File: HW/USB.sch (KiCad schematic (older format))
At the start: 6 parts

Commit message: remove pin from USB
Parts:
- removed D?: D_Schottky, symbol Device:D_Schottky
- removed J?: +5V_USB, symbol Connector:Conn_01x01_Male
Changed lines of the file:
@@
 $Descr A4 11693 8268
 encoding utf-8
-Sheet 17 42
+Sheet 15 42
 Title ""
 Date ""
@@
 	4300 3250 4350 3250
 Wire Wire Line
-	4300 2950 4400 2950
+	4300 2950 4650 2950
 $Comp
 L Diode:SD05_SOD323 D?
@@
 	4500 3150 4300 3150
 $Comp
-L Device:D_Schottky D?
-U 1 1 5F7931B4
-P 4650 2650
-AR Path="/5FBB3550/5F7931B4" Ref="D?"  Part="1"
-AR Path="/5F7931B4" Ref="D?"  Part="1"
-AR Path="/5F78DB3E/5F7931B4" Ref="D?"  Part="1"
-F 0 "D?" V 4604 2730 50  0000 L CNN
-F 1 "D_Schottky" V 4695 2730 50  0000 L CNN
-F 2 "" H 4650 2650 50  0001 C CNN
-F 3 "~" H 4650 2650 50  0001 C CNN
-	1    4650 2650
-	0    1    1    0
-$EndComp
-Wire Wire Line
-	4650 2800 4650 2950
-$Comp
-L Connector:Conn_01x01_Male J?
-U 1 1 5F7931BB
-P 4650 2150
-AR Path="/5FBB3550/5F7931BB" Ref="J?"  Part="1"
-AR Path="/5F7931BB" Ref="J?"  Part="1"
-AR Path="/5F78DB3E/5F7931BB" Ref="J?"  Part="1"
-F 0 "J?" V 4712 2194 50  0000 L CNN
-F 1 "+5V_USB" V 4803 2194 50  0000 L CNN
-F 2 "" H 4650 2150 50  0001 C CNN
-F 3 "~" H 4650 2150 50  0001 C CNN
-	1    4650 2150
-	0    1    1    0
-$EndComp
-Wire Wire Line
-	4650 2350 4650 2500
-$Comp
 L power:GND #PWR?
 U 1 1 5F7931C2
@@
 L power:+5V #PWR?
 U 1 1 5F7931CC
-P 4400 2850
+P 4650 2800
 AR Path="/5F7931CC" Ref="#PWR?"  Part="1"
 AR Path="/5F78DB3E/5F7931CC" Ref="#PWR?"  Part="1"
-F 0 "#PWR?" H 4400 2700 50  0001 C CNN
-F 1 "+5V" H 4415 3023 50  0000 C CNN
-F 2 "" H 4400 2850 50  0001 C CNN
-F 3 "" H 4400 2850 50  0001 C CNN
-	1    4400 2850
+F 0 "#PWR?" H 4650 2650 50  0001 C CNN
+F 1 "+5V" H 4665 2973 50  0000 C CNN
+F 2 "" H 4650 2800 50  0001 C CNN
+F 3 "" H 4650 2800 50  0001 C CNN
+	1    4650 2800
 	1    0    0    -1
 $EndComp
 Wire Wire Line
-	4400 2850 4400 2950
-Connection ~ 4400 2950
-Wire Wire Line
-	4400 2950 4650 2950
+	4650 2800 4650 2950
 $EndSCHEMATC

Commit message: add some packages
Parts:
- J?: footprint (none) -> Connector_USB:USB_Micro-B_Wuerth_629105150521
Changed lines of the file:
@@
 F 0 "J?" H 4057 3617 50  0000 C CNN
 F 1 "USB_B_Micro" H 4057 3526 50  0000 C CNN
-F 2 "" H 4150 3100 50  0001 C CNN
+F 2 "Connector_USB:USB_Micro-B_Wuerth_629105150521" H 4150 3100 50  0001 C CNN
 F 3 "~" H 4150 3100 50  0001 C CNN
 	1    4000 3150

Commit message: add footprint of inductor, add codes for JLCPCB, repair mistakes
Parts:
- D? (x3): LCSC (none) -> neosazovat
- J?: LCSC (none) -> ručně
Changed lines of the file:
@@
 F 2 "Connector_USB:USB_Micro-B_Wuerth_629105150521" H 4150 3100 50  0001 C CNN
 F 3 "~" H 4150 3100 50  0001 C CNN
+F 4 "ručně" H 4000 3150 50  0001 C CNN "LCSC"
 	1    4000 3150
 	1    0    0    -1
@@
 F 2 "Diode_SMD:D_SOD-323" H 4350 3450 50  0001 C CNN
 F 3 "https://www.littelfuse.com/~/media/electronics/datasheets/tvs_diode_arrays/littelfuse_tvs_diode_array_sd_c_datasheet.pdf.pdf" H 4350 3650 50  0001 C CNN
+F 4 "neosazovat" H 4350 3650 50  0001 C CNN "LCSC"
 	1    4350 3650
 	0    -1   -1   0
@@
 F 2 "Diode_SMD:D_SOD-323" H 4500 3450 50  0001 C CNN
 F 3 "https://www.littelfuse.com/~/media/electronics/datasheets/tvs_diode_arrays/littelfuse_tvs_diode_array_sd_c_datasheet.pdf.pdf" H 4500 3650 50  0001 C CNN
+F 4 "neosazovat" H 4500 3650 50  0001 C CNN "LCSC"
 	1    4500 3650
 	0    -1   -1   0
@@
 F 2 "Diode_SMD:D_SOD-323" H 4650 3450 50  0001 C CNN
 F 3 "https://www.littelfuse.com/~/media/electronics/datasheets/tvs_diode_arrays/littelfuse_tvs_diode_array_sd_c_datasheet.pdf.pdf" H 4650 3650 50  0001 C CNN
+F 4 "neosazovat" H 4650 3650 50  0001 C CNN "LCSC"
 	1    4650 3650
 	0    -1   -1   0

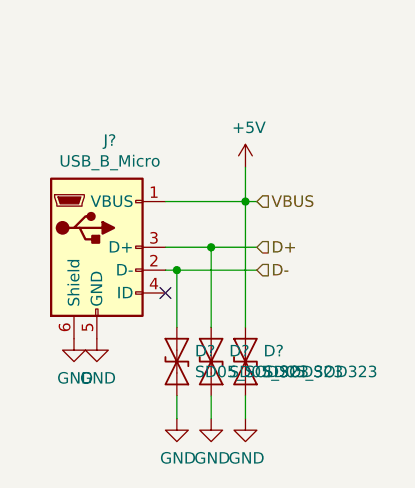
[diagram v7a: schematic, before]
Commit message: numbering components, place components on board
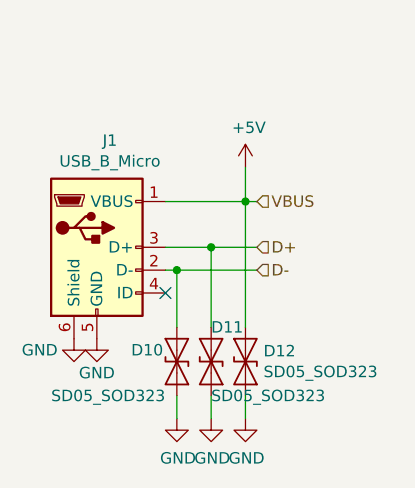
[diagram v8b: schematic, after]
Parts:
- gave numbers to parts that had none: 4
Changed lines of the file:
@@
 AR Path="/5F793175" Ref="J?"  Part="1"
 AR Path="/5FBB3550/5F793175" Ref="J?"  Part="1"
-AR Path="/5F78DB3E/5F793175" Ref="J?"  Part="1"
-F 0 "J?" H 4057 3617 50  0000 C CNN
+AR Path="/5F78DB3E/5F793175" Ref="J1"  Part="1"
+F 0 "J1" H 4057 3617 50  0000 C CNN
 F 1 "USB_B_Micro" H 4057 3526 50  0000 C CNN
 F 2 "Connector_USB:USB_Micro-B_Wuerth_629105150521" H 4150 3100 50  0001 C CNN
@@
 AR Path="/5FBB3550/5F79317B" Ref="#PWR?"  Part="1"
 AR Path="/5F79317B" Ref="#PWR?"  Part="1"
-AR Path="/5F78DB3E/5F79317B" Ref="#PWR?"  Part="1"
-F 0 "#PWR?" H 4000 3300 50  0001 C CNN
-F 1 "GND" H 4005 3377 50  0000 C CNN
+AR Path="/5F78DB3E/5F79317B" Ref="#PWR0148"  Part="1"
+F 0 "#PWR0148" H 4000 3300 50  0001 C CNN
+F 1 "GND" H 4000 3400 50  0000 C CNN
 F 2 "" H 4000 3550 50  0001 C CNN
 F 3 "" H 4000 3550 50  0001 C CNN
@@
 AR Path="/5FBB3550/5F793184" Ref="D?"  Part="1"
 AR Path="/5F793184" Ref="D?"  Part="1"
-AR Path="/5F78DB3E/5F793184" Ref="D?"  Part="1"
-F 0 "D?" V 4396 3571 50  0000 R CNN
-F 1 "SD05_SOD323" V 4305 3571 50  0000 R CNN
+AR Path="/5F78DB3E/5F793184" Ref="D10"  Part="1"
+F 0 "D10" V 4400 3850 50  0000 R CNN
+F 1 "SD05_SOD323" V 4200 4200 50  0000 R CNN
 F 2 "Diode_SMD:D_SOD-323" H 4350 3450 50  0001 C CNN
 F 3 "https://www.littelfuse.com/~/media/electronics/datasheets/tvs_diode_arrays/littelfuse_tvs_diode_array_sd_c_datasheet.pdf.pdf" H 4350 3650 50  0001 C CNN
@@
 AR Path="/5FBB3550/5F79318A" Ref="D?"  Part="1"
 AR Path="/5F79318A" Ref="D?"  Part="1"
-AR Path="/5F78DB3E/5F79318A" Ref="D?"  Part="1"
-F 0 "D?" V 4546 3571 50  0000 R CNN
-F 1 "SD05_SOD323" V 4455 3571 50  0000 R CNN
+AR Path="/5F78DB3E/5F79318A" Ref="D11"  Part="1"
+F 0 "D11" V 4650 3650 50  0000 R CNN
+F 1 "SD05_SOD323" V 4350 3650 50  0000 R CNN
 F 2 "Diode_SMD:D_SOD-323" H 4500 3450 50  0001 C CNN
 F 3 "https://www.littelfuse.com/~/media/electronics/datasheets/tvs_diode_arrays/littelfuse_tvs_diode_array_sd_c_datasheet.pdf.pdf" H 4500 3650 50  0001 C CNN
@@
 AR Path="/5FBB3550/5F793190" Ref="D?"  Part="1"
 AR Path="/5F793190" Ref="D?"  Part="1"
-AR Path="/5F78DB3E/5F793190" Ref="D?"  Part="1"
-F 0 "D?" V 4696 3571 50  0000 R CNN
+AR Path="/5F78DB3E/5F793190" Ref="D12"  Part="1"
+F 0 "D12" V 4696 3571 50  0000 R CNN
 F 1 "SD05_SOD323" V 4605 3571 50  0000 R CNN
 F 2 "Diode_SMD:D_SOD-323" H 4650 3450 50  0001 C CNN
@@
 AR Path="/5FBB3550/5F793196" Ref="#PWR?"  Part="1"
 AR Path="/5F793196" Ref="#PWR?"  Part="1"
-AR Path="/5F78DB3E/5F793196" Ref="#PWR?"  Part="1"
-F 0 "#PWR?" H 4350 3650 50  0001 C CNN
+AR Path="/5F78DB3E/5F793196" Ref="#PWR0149"  Part="1"
+F 0 "#PWR0149" H 4350 3650 50  0001 C CNN
 F 1 "GND" H 4355 3727 50  0000 C CNN
 F 2 "" H 4350 3900 50  0001 C CNN
@@
 AR Path="/5FBB3550/5F79319C" Ref="#PWR?"  Part="1"
 AR Path="/5F79319C" Ref="#PWR?"  Part="1"
-AR Path="/5F78DB3E/5F79319C" Ref="#PWR?"  Part="1"
-F 0 "#PWR?" H 4500 3650 50  0001 C CNN
+AR Path="/5F78DB3E/5F79319C" Ref="#PWR0150"  Part="1"
+F 0 "#PWR0150" H 4500 3650 50  0001 C CNN
 F 1 "GND" H 4505 3727 50  0000 C CNN
 F 2 "" H 4500 3900 50  0001 C CNN
@@
 AR Path="/5FBB3550/5F7931A2" Ref="#PWR?"  Part="1"
 AR Path="/5F7931A2" Ref="#PWR?"  Part="1"
-AR Path="/5F78DB3E/5F7931A2" Ref="#PWR?"  Part="1"
-F 0 "#PWR?" H 4650 3650 50  0001 C CNN
+AR Path="/5F78DB3E/5F7931A2" Ref="#PWR0151"  Part="1"
+F 0 "#PWR0151" H 4650 3650 50  0001 C CNN
 F 1 "GND" H 4655 3727 50  0000 C CNN
 F 2 "" H 4650 3900 50  0001 C CNN
@@
 AR Path="/5FBB3550/5F7931C2" Ref="#PWR?"  Part="1"
 AR Path="/5F7931C2" Ref="#PWR?"  Part="1"
-AR Path="/5F78DB3E/5F7931C2" Ref="#PWR?"  Part="1"
-F 0 "#PWR?" H 3900 3300 50  0001 C CNN
-F 1 "GND" H 3905 3377 50  0000 C CNN
+AR Path="/5F78DB3E/5F7931C2" Ref="#PWR0152"  Part="1"
+F 0 "#PWR0152" H 3900 3300 50  0001 C CNN
+F 1 "GND" H 3750 3500 50  0000 C CNN
 F 2 "" H 3900 3550 50  0001 C CNN
 F 3 "" H 3900 3550 50  0001 C CNN
@@
 P 4650 2800
 AR Path="/5F7931CC" Ref="#PWR?"  Part="1"
-AR Path="/5F78DB3E/5F7931CC" Ref="#PWR?"  Part="1"
-F 0 "#PWR?" H 4650 2650 50  0001 C CNN
+AR Path="/5F78DB3E/5F7931CC" Ref="#PWR0153"  Part="1"
+F 0 "#PWR0153" H 4650 2650 50  0001 C CNN
 F 1 "+5V" H 4665 2973 50  0000 C CNN
 F 2 "" H 4650 2800 50  0001 C CNN
